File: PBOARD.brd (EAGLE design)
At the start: 80 x 46 mm, 11 parts, among them J1 POWER_JACKPTH_SLOTS, J10 POWER_JACKPTH_SLOTS, J2 POWER_JACKPTH_SLOTS, J3 POWER_JACKPTH_SLOTS, J4 POWER_JACKPTH_SLOTS, J5 POWER_JACKPTH_SLOTS, J7 POWER_JACKPTH_SLOTS, J8 POWER_JACKPTH_SLOTS, J9 POWER_JACKPTH_SLOTS

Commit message: Merged files from PowerDistributionBoard project
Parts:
- removed J10: POWER_JACKPTH_SLOTS, freetronics-jon:POWER_JACK_PTH_SLOTS
- removed LED1: GREEN, freetronics-jon:LED3MM
- removed R1: 1K, freetronics-jon:AXIAL-0.3
- added J6: POWER_JACKPTH_SLOTS, freetronics-jon:POWER_JACK_PTH_SLOTS
- added JP1: (no value), freetronics-jon:SCREWTERMINAL-5MM-2
- moved J1 66.2 mm to (27.0, -3.00), turned to 0 degrees
- moved J5 42.0 mm to (54.0, 49.0)
- moved J2 40.5 mm to (13.5, 49.0)
- moved J7 27.5 mm to (40.5, -3.00)
- moved J9 27.5 mm to (67.5, -3.00)
- moved J4 14.5 mm to (40.5, 49.0)
- moved J3 13.0 mm to (27.0, 49.0)
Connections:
- removed net 3.3V: J1.PWR, J10.PWR, J2.PWR, J3.PWR, J4.PWR, J5.PWR, J7.PWR, J8.PWR, J9.PWR, R1.P$1
- removed net N$1: LED1.A, R1.P$2
- new net VCC: J1.PWR, J2.PWR, J3.PWR, J4.PWR, J5.PWR, J6.PWR, J7.PWR, J8.PWR, J9.PWR, JP1.2
- net GND: now also J6.GND, J6.GNDBREAK, JP1.1; no longer J10.GND, J10.GNDBREAK, LED1.K
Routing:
- net VCC: track 0.00 -> 148.2 mm
- net 3.3V: track 144.2 -> 0.00 mm
- net N$1: track 6.72 -> 0.00 mm
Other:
- board size 80 x 46 mm -> 81 x 46 mm
- board text added: "Copyright 2018 SuperHouse Automation Pty Ltd www.superhouse.tv"
- board text added: "Released under the TAPR Open Hardware License: tapr.org/OHL"
- board text removed: "+"
- board text removed: "-"
- board text removed: "1"
- board text removed: "2"
- board text removed: "3"
- board text removed: "4"
- board text removed: "5V FTDI"
- board text removed: "7.4V LiPo"
- board text removed: "A0: CH1 A1: CH2 A2: CH3 A3: CH4 A6: VBAT"
- board text removed: "ATmega328P 16MHz"
- board text removed: "AntBrain"
- board text removed: "D11: LA D12: LB D9: RA D10: RB D13: LED"
- board text removed: "D13"
- board text removed: "L1"
- board text removed: "PWR"
- board text removed: "SW1"
- board text removed: "SWITCH"
- board text removed: "Select "Arduino Uno" in Arduino IDE"
- board text removed: "freetronics"
- board text removed: "tron.cc/antbrain"

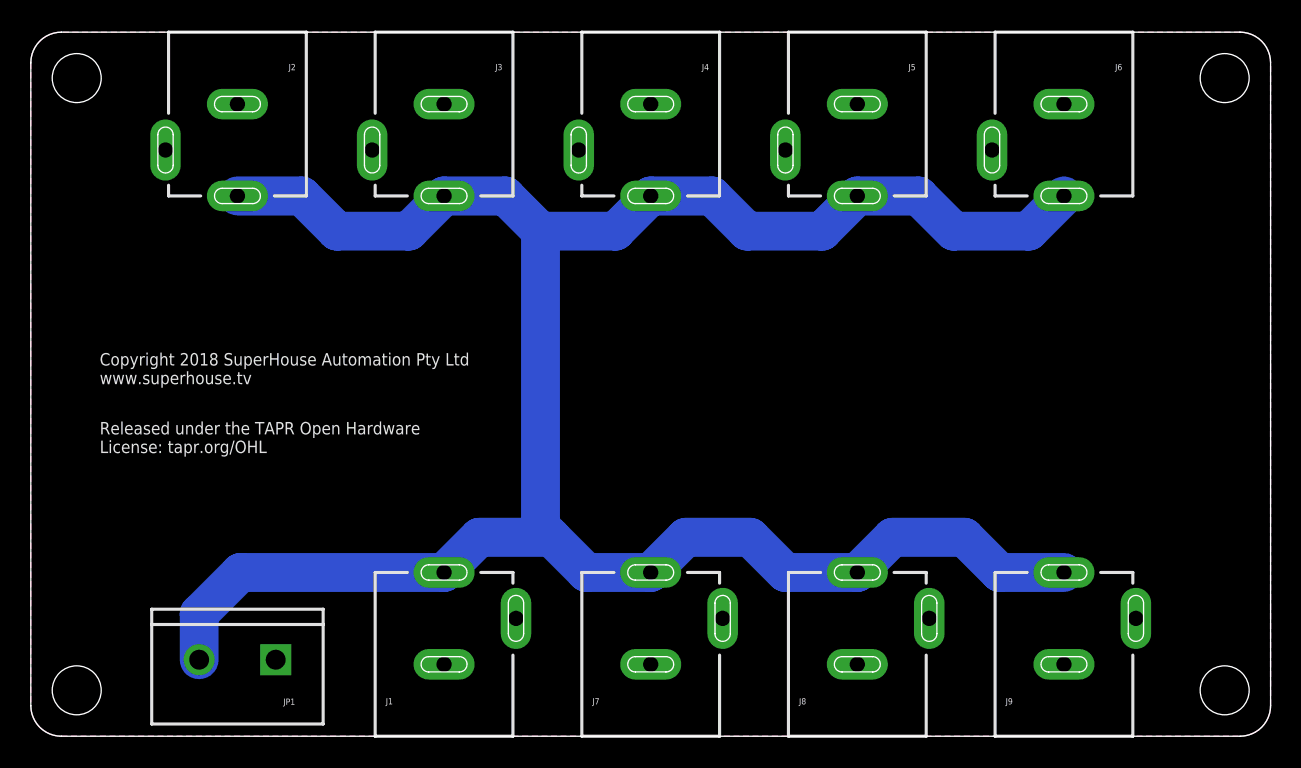
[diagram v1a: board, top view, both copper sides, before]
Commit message: Added power LED for v1.0 release
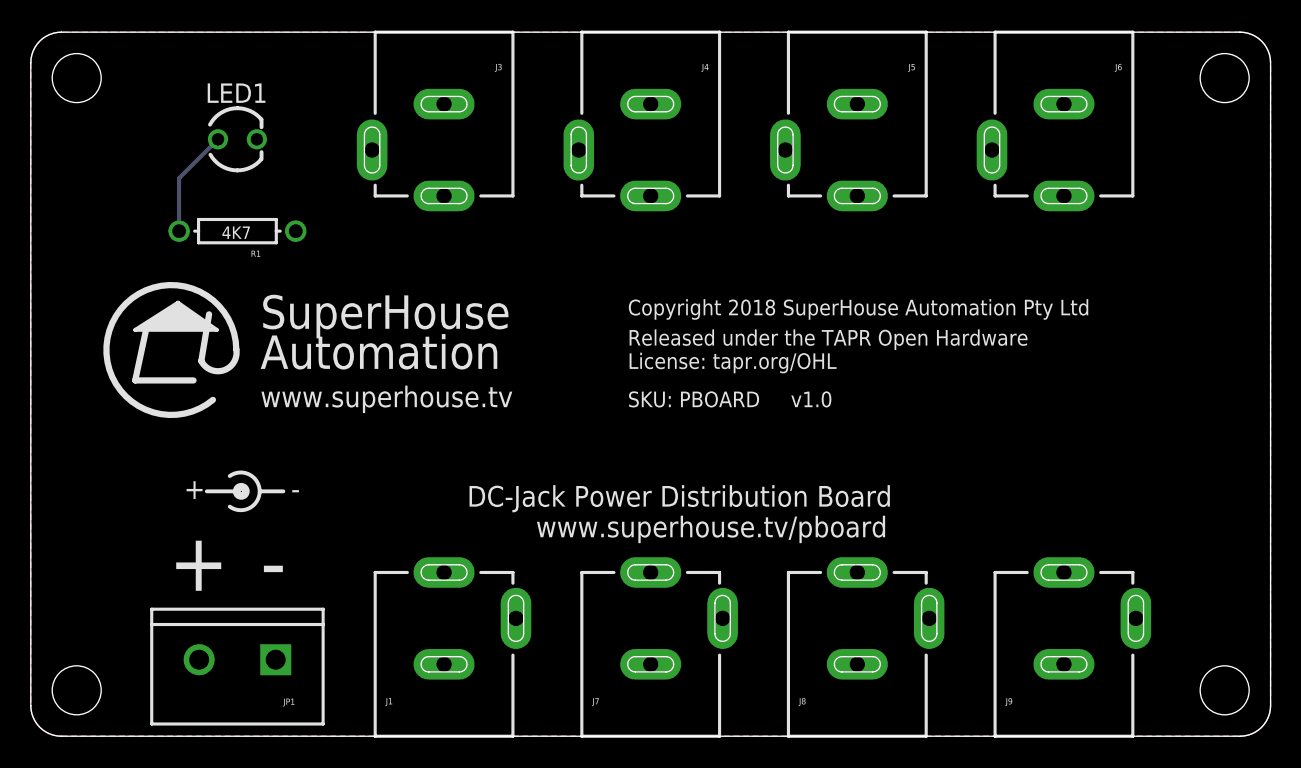
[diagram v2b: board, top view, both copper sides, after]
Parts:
- removed J2: POWER_JACKPTH_SLOTS, freetronics-jon:POWER_JACK_PTH_SLOTS
- added LED1: BLUE, freetronics-jon:LED3MM
- added R1: 4K7, freetronics-jon:AXIAL-0.3
- JP1: value (none) -> POWER IN
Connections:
- new net N$1: LED1.A, R1.P$1
- net GND: now also LED1.K; no longer J2.GND, J2.GNDBREAK
- net VCC: now also R1.P$2; no longer J2.PWR
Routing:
- net VCC: track 148.2 -> 0.00 mm
- net N$1: track 0.00 -> 7.05 mm
- added copper zone on layer 16, net VCC
- removed copper zone on layer 16, net GND
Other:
- board text added: "+"
- board text added: "-"
- board text added: "Copyright 2018 SuperHouse Automation Pty Ltd"
- board text added: "DC-Jack Power Distribution Board"
- board text added: "SKU: PBOARD v1.0"
- board text added: "SuperHouse Automation"
- board text added: "www.superhouse.tv"
- board text added: "www.superhouse.tv/pboard"
- board text removed: "Copyright 2018 SuperHouse Automation Pty Ltd www.superhouse.tv"
